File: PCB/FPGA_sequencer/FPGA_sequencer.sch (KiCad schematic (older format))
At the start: 33 parts, among them U1 ADA4940-2ACPZ-R7_a, U2 AD9648BCPZ-125, U3 DB3S406F0L, U4 DB3S406F0L

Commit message: pass capacitor add
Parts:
- 10n1, C1, C10, C11, C12, C13, C14, C15, C2, C3, C4, C5, C6, C7, C8, C9: footprint Capacitor_SMD:C_0603_1608Metric -> Capacitors_SMD:C_0603
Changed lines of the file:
@@
 F 0 "C1" V 7071 1700 50  0000 C CNN
 F 1 "22p" V 7162 1700 50  0000 C CNN
-F 2 "Capacitor_SMD:C_0603_1608Metric" H 7300 1700 50  0001 C CNN
+F 2 "Capacitors_SMD:C_0603" H 7300 1700 50  0001 C CNN
 F 3 "~" H 7300 1700 50  0001 C CNN
 	1    7300 1700
@@
 F 0 "C2" V 7571 1700 50  0000 C CNN
 F 1 "22p" V 7662 1700 50  0000 C CNN
-F 2 "Capacitor_SMD:C_0603_1608Metric" H 7800 1700 50  0001 C CNN
+F 2 "Capacitors_SMD:C_0603" H 7800 1700 50  0001 C CNN
 F 3 "~" H 7800 1700 50  0001 C CNN
 	1    7800 1700
@@
 F 0 "C11" H 3808 4704 50  0000 R CNN
 F 1 "0.1u" H 3808 4795 50  0000 R CNN
-F 2 "Capacitor_SMD:C_0603_1608Metric" H 3900 4750 50  0001 C CNN
+F 2 "Capacitors_SMD:C_0603" H 3900 4750 50  0001 C CNN
 F 3 "~" H 3900 4750 50  0001 C CNN
 	1    3900 4750
@@
 F 0 "C9" H 3508 4704 50  0000 R CNN
 F 1 "0.1u" H 3508 4795 50  0000 R CNN
-F 2 "Capacitor_SMD:C_0603_1608Metric" H 3600 4750 50  0001 C CNN
+F 2 "Capacitors_SMD:C_0603" H 3600 4750 50  0001 C CNN
 F 3 "~" H 3600 4750 50  0001 C CNN
 	1    3600 4750
@@
 F 0 "C7" H 3158 4704 50  0000 R CNN
 F 1 "0.1u" H 3158 4795 50  0000 R CNN
-F 2 "Capacitor_SMD:C_0603_1608Metric" H 3250 4750 50  0001 C CNN
+F 2 "Capacitors_SMD:C_0603" H 3250 4750 50  0001 C CNN
 F 3 "~" H 3250 4750 50  0001 C CNN
 	1    3250 4750
@@
 F 0 "C12" H 3808 5004 50  0000 R CNN
 F 1 "0.1u" H 3808 5095 50  0000 R CNN
-F 2 "Capacitor_SMD:C_0603_1608Metric" H 3900 5050 50  0001 C CNN
+F 2 "Capacitors_SMD:C_0603" H 3900 5050 50  0001 C CNN
 F 3 "~" H 3900 5050 50  0001 C CNN
 	1    3900 5050
@@
 F 0 "C10" H 3508 5004 50  0000 R CNN
 F 1 "0.1u" H 3508 5095 50  0000 R CNN
-F 2 "Capacitor_SMD:C_0603_1608Metric" H 3600 5050 50  0001 C CNN
+F 2 "Capacitors_SMD:C_0603" H 3600 5050 50  0001 C CNN
 F 3 "~" H 3600 5050 50  0001 C CNN
 	1    3600 5050
@@
 F 0 "C8" H 3158 5004 50  0000 R CNN
 F 1 "0.1u" H 3158 5095 50  0000 R CNN
-F 2 "Capacitor_SMD:C_0603_1608Metric" H 3250 5050 50  0001 C CNN
+F 2 "Capacitors_SMD:C_0603" H 3250 5050 50  0001 C CNN
 F 3 "~" H 3250 5050 50  0001 C CNN
 	1    3250 5050
@@
 F 0 "C3" H 2508 4704 50  0000 R CNN
 F 1 "10u" H 2508 4795 50  0000 R CNN
-F 2 "Capacitor_SMD:C_0603_1608Metric" H 2600 4750 50  0001 C CNN
+F 2 "Capacitors_SMD:C_0603" H 2600 4750 50  0001 C CNN
 F 3 "~" H 2600 4750 50  0001 C CNN
 	1    2600 4750
@@
 F 0 "C4" H 2508 5004 50  0000 R CNN
 F 1 "10u" H 2508 5095 50  0000 R CNN
-F 2 "Capacitor_SMD:C_0603_1608Metric" H 2600 5050 50  0001 C CNN
+F 2 "Capacitors_SMD:C_0603" H 2600 5050 50  0001 C CNN
 F 3 "~" H 2600 5050 50  0001 C CNN
 	1    2600 5050
@@
 F 0 "C5" H 2858 4704 50  0000 R CNN
 F 1 "1u" H 2858 4795 50  0000 R CNN
-F 2 "Capacitor_SMD:C_0603_1608Metric" H 2950 4750 50  0001 C CNN
+F 2 "Capacitors_SMD:C_0603" H 2950 4750 50  0001 C CNN
 F 3 "~" H 2950 4750 50  0001 C CNN
 	1    2950 4750
@@
 F 0 "C6" H 2858 5004 50  0000 R CNN
 F 1 "1u" H 2858 5095 50  0000 R CNN
-F 2 "Capacitor_SMD:C_0603_1608Metric" H 2950 5050 50  0001 C CNN
+F 2 "Capacitors_SMD:C_0603" H 2950 5050 50  0001 C CNN
 F 3 "~" H 2950 5050 50  0001 C CNN
 	1    2950 5050
@@
 F 0 "C14" H 4458 4704 50  0000 R CNN
 F 1 "10n" H 4458 4795 50  0000 R CNN
-F 2 "Capacitor_SMD:C_0603_1608Metric" H 4550 4750 50  0001 C CNN
+F 2 "Capacitors_SMD:C_0603" H 4550 4750 50  0001 C CNN
 F 3 "~" H 4550 4750 50  0001 C CNN
 	1    4550 4750
@@
 F 0 "C13" H 4158 4704 50  0000 R CNN
 F 1 "10n" H 4158 4795 50  0000 R CNN
-F 2 "Capacitor_SMD:C_0603_1608Metric" H 4250 4750 50  0001 C CNN
+F 2 "Capacitors_SMD:C_0603" H 4250 4750 50  0001 C CNN
 F 3 "~" H 4250 4750 50  0001 C CNN
 	1    4250 4750
@@
 F 0 "C15" H 4458 5004 50  0000 R CNN
 F 1 "10n" H 4458 5095 50  0000 R CNN
-F 2 "Capacitor_SMD:C_0603_1608Metric" H 4550 5050 50  0001 C CNN
+F 2 "Capacitors_SMD:C_0603" H 4550 5050 50  0001 C CNN
 F 3 "~" H 4550 5050 50  0001 C CNN
 	1    4550 5050
@@
 F 0 "10n1" H 4158 5004 50  0000 R CNN
 F 1 "0.1u" H 4158 5095 50  0000 R CNN
-F 2 "Capacitor_SMD:C_0603_1608Metric" H 4250 5050 50  0001 C CNN
+F 2 "Capacitors_SMD:C_0603" H 4250 5050 50  0001 C CNN
 F 3 "~" H 4250 5050 50  0001 C CNN
 	1    4250 5050

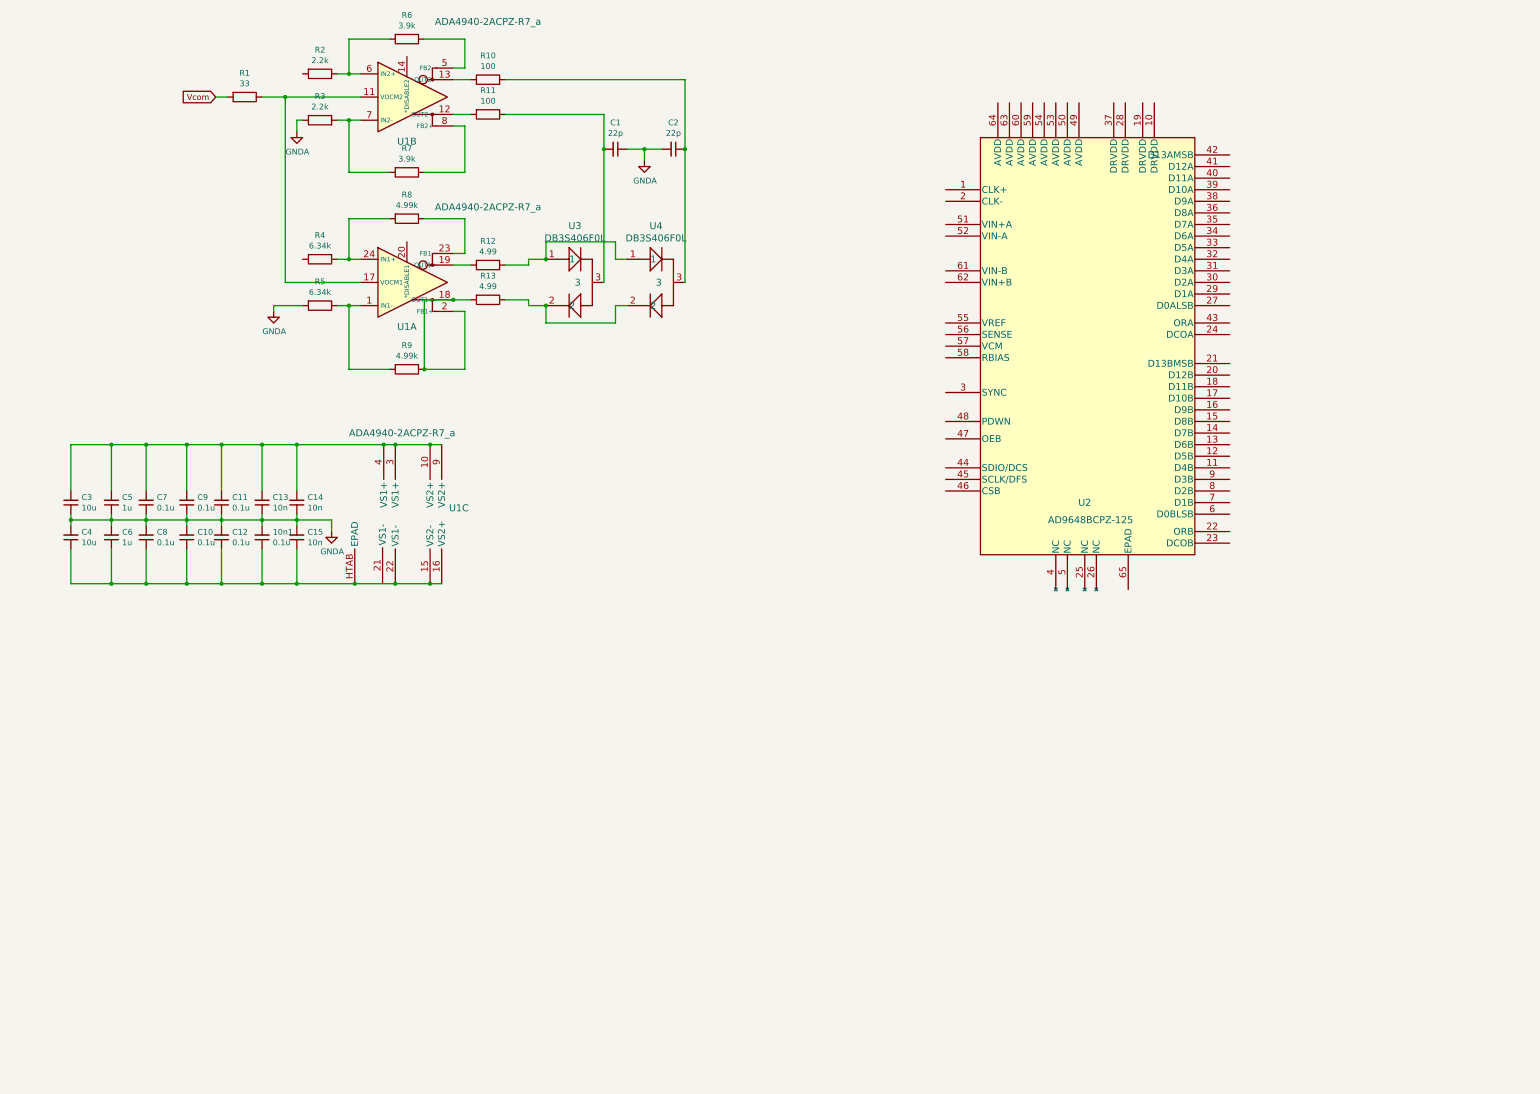
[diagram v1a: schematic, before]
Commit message: AD8065 add
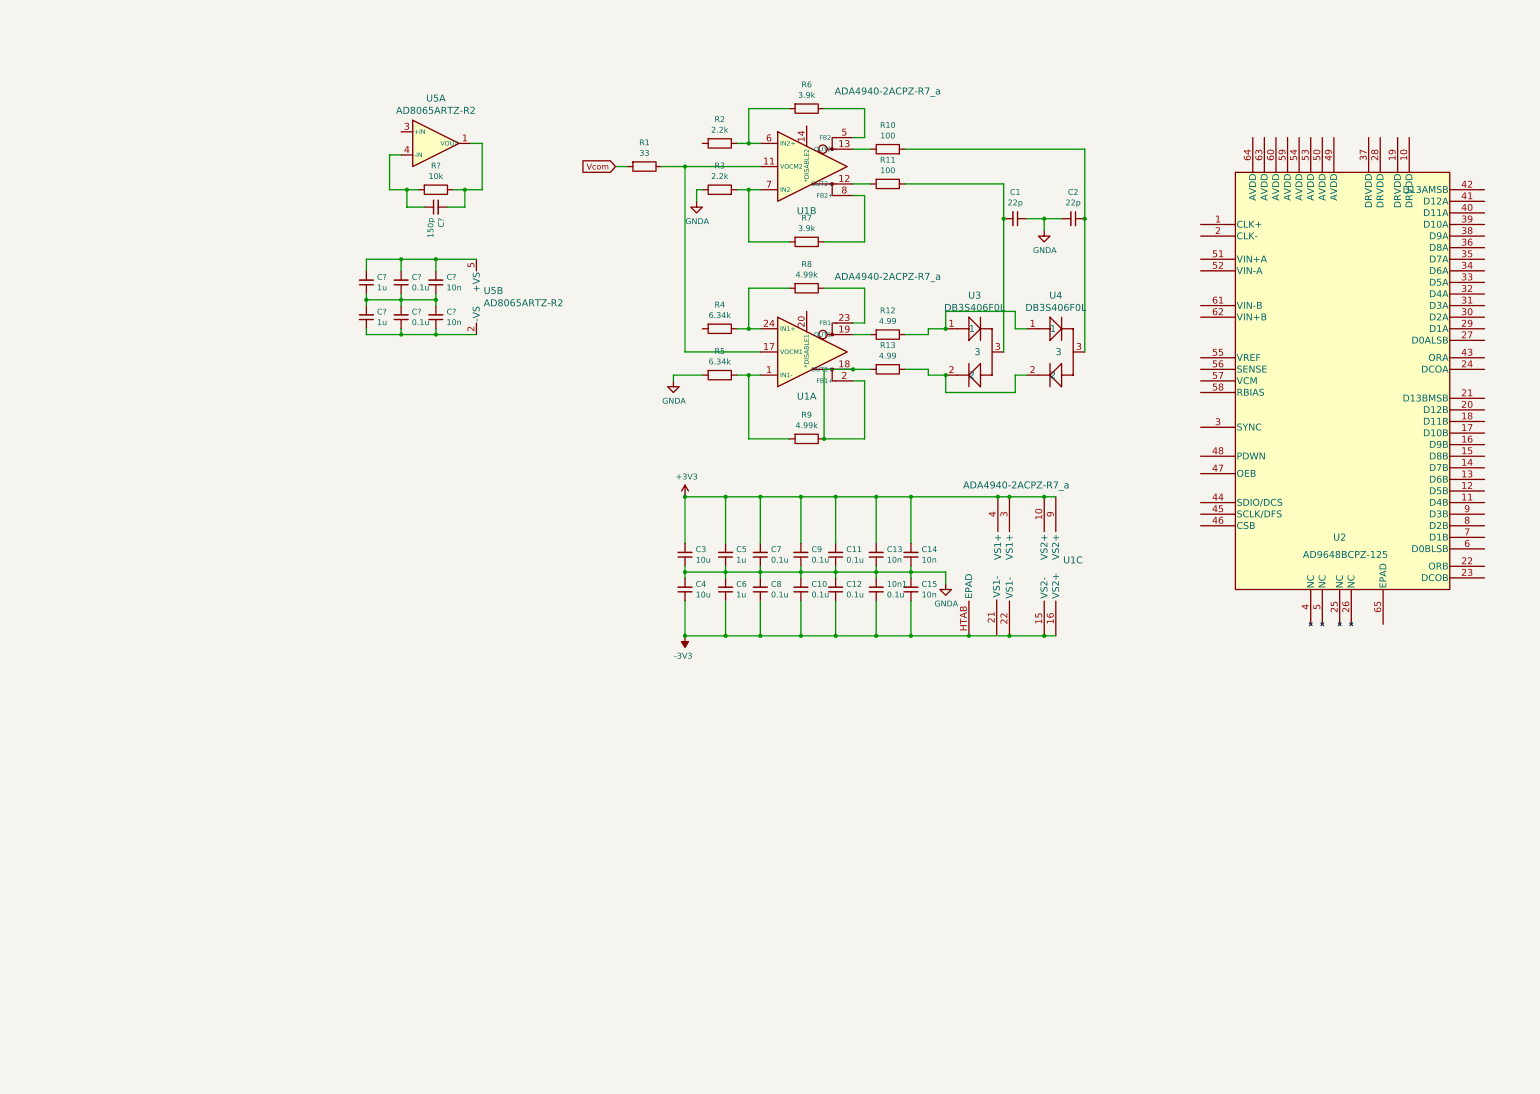
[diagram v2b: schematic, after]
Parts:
- added C? (x2): 0.1u, Capacitors_SMD:C_0603, symbol Device:C_Small
- added C? (x2): 10n, Capacitors_SMD:C_0603, symbol Device:C_Small
- added C? (x2): 1u, Capacitors_SMD:C_0603, symbol Device:C_Small
- added C?: 150p, Capacitors_SMD:C_0603, symbol Device:C_Small
- added R?: 10k, Resistor_SMD:R_0603_1608Metric, symbol Device:R
- added U5: AD8065ARTZ-R2, FPGA_sequencer:AD8065ARTZ-R2, symbol FPGA_sequencer:AD8065ARTZ-R2
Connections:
- net +3V3: now reaches C11.2, C13.2, C14.2, C3.2, C5.2, C7.2, C9.2, U1.10 (VS2+), U1.3 (VS1+), U1.4 (VS1+), U1.9 (VS2+)
- net -3V3: now reaches 10n1.1, C10.1, C12.1, C15.1, C4.1, C6.1, C8.1, U1.15 (VS2-), U1.16 (VS2+), U1.22 (VS1-), U1.HTAB (EPAD)
- new net: C?.2, R?.1, U5.1 (VOUT)
- new net: C?.1, R?.2, U5.4 (-IN)
- new net: C?.1, C?.1, C?.1, U5.2 (-VS)
- new net: C?.2, C?.2, C?.2, U5.5 (+VS)
- new net: C?.1, C?.1, C?.1, C?.2, C?.2, C?.2
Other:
- moved on the sheet: 10n1, C1, C10, C11, C12, C13, C14, C15, C2, C3, C4, C5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

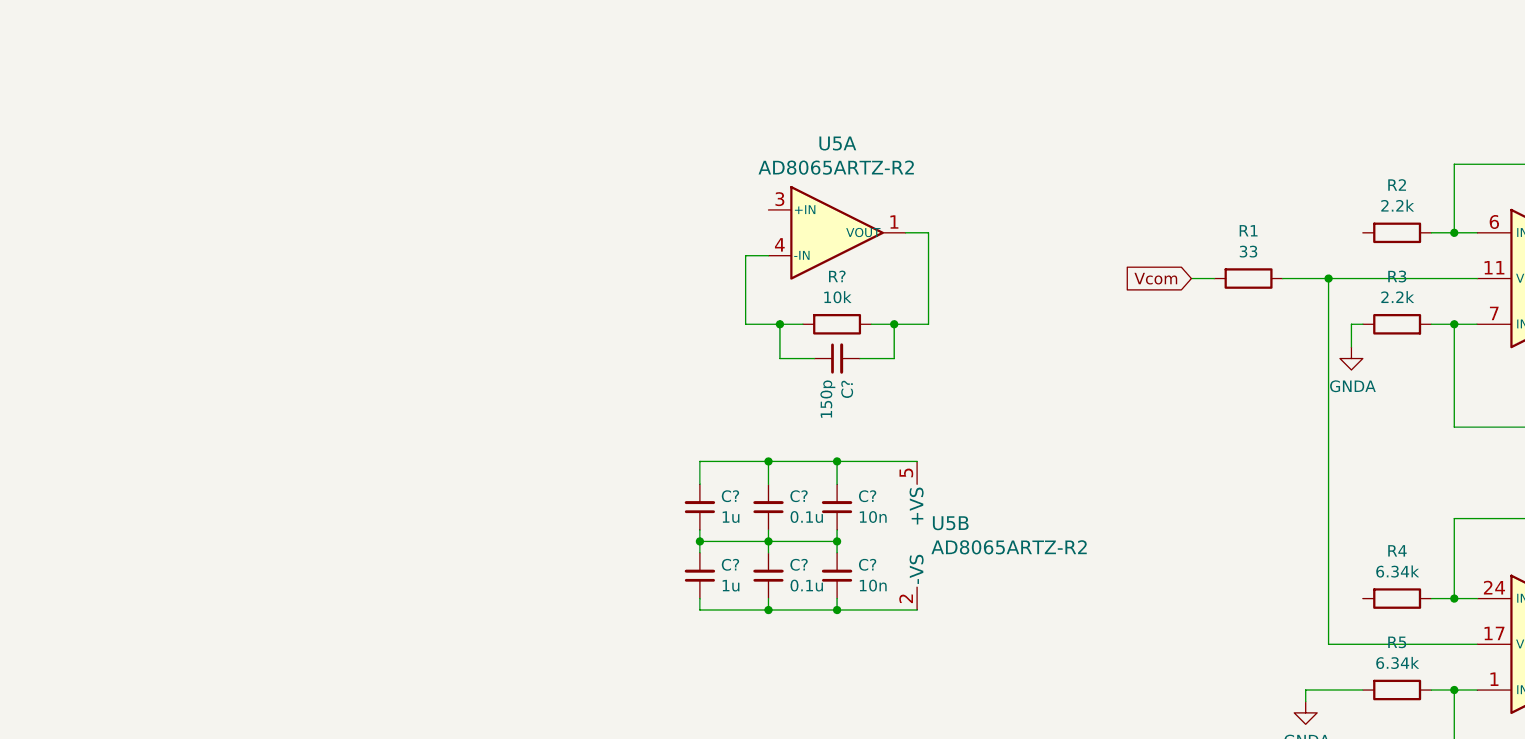
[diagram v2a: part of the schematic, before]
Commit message: MAX4565 Analog switch add
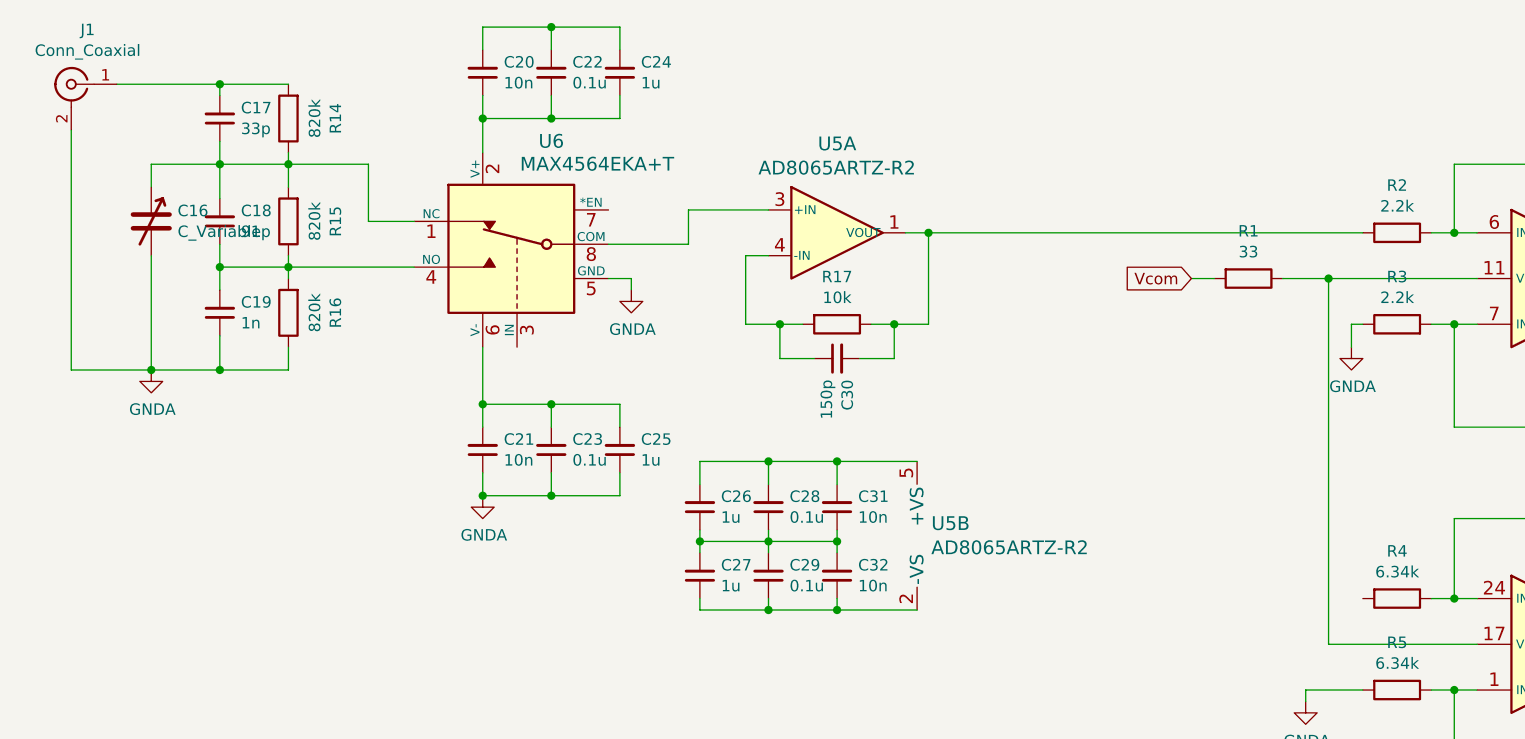
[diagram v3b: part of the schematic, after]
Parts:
- added C16: C_Variable, Capacitor_SMD:C_Trimmer_Murata_TZB4-A, symbol Device:C_Variable
- added C17: 33p, Capacitor_SMD:C_0201_0603Metric, symbol Device:C_Small
- added C18: 91p, Capacitor_SMD:C_0201_0603Metric, symbol Device:C_Small
- added C19: 1n, Capacitor_SMD:C_0201_0603Metric, symbol Device:C_Small
- added C20, C21: 10n, Capacitor_SMD:C_0201_0603Metric, symbol Device:C_Small
- added C22, C23: 0.1u, Capacitor_SMD:C_0201_0603Metric, symbol Device:C_Small
- added C24, C25: 1u, Capacitor_SMD:C_0201_0603Metric, symbol Device:C_Small
- added J1: Conn_Coaxial, Connector_Coaxial:SMA_Amphenol_132134-11_Vertical, symbol Connector:Conn_Coaxial
- added R14, R15, R16: 820k, Resistor_SMD:R_0603_1608Metric, symbol Device:R
- added U6: MAX4564EKA+T, FPGA_sequencer:MAX4564EKA&plus_T, symbol FPGA_sequencer:MAX4564EKA+T
- 10n1, C1, C10, C11, C12, C13, C14, C15, C2, C3, C4, C5, C6, C7, C8, C9: footprint Capacitors_SMD:C_0603 -> Capacitor_SMD:C_0201_0603Metric
- C26, C27, C28, C29, C30, C31, C32: renamed from C?; footprint Capacitors_SMD:C_0603 -> Capacitor_SMD:C_0201_0603Metric
- gave numbers to parts that had none: 1
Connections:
- net GNDA: now also C16.2, C19.1, C21.1, C23.1, C25.1, J1.2 (Ext), R16.1, U6.5 (GND)
- net at C30.2, R17.1, U5.1 (VOUT): now also R2.2
- net at U5.3 (+IN): now also U6.8 (COM)
- new net: C16.1, C17.1, C18.2, R14.1, R15.2, U6.1 (NC)
- new net: C20.1, C22.1, C24.1, U6.2 (V+)
- new net: C18.1, C19.2, R15.1, R16.2, U6.4 (NO)
- new net: C21.2, C23.2, C25.2, U6.6 (V-)
- new net: C17.2, J1.1 (In), R14.2
- new net: C20.2, C22.2, C24.2

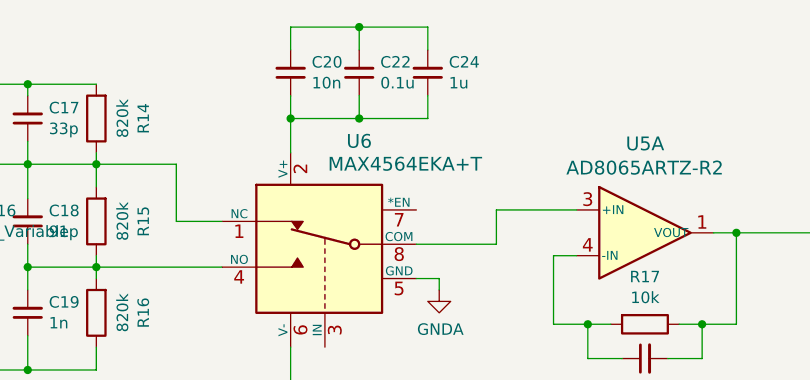
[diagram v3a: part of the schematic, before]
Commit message: ADC driver pattern write
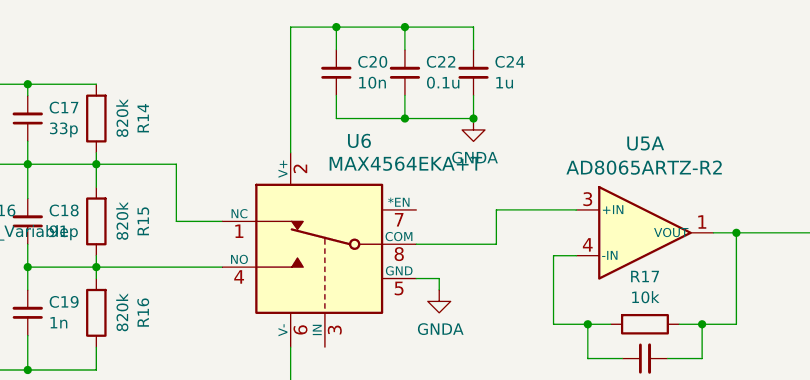
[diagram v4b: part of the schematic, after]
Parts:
- 10n1, C1, C10, C11, C12, C13, C14, C15, C17, C18, C19, C2, C20, C21, C22, C23, C24, C25, C26, C27, C28, C29, C3, C30, C31, C32, C4, C5, C6, C7, C8, C9: footprint Capacitor_SMD:C_0201_0603Metric -> Capacitor_SMD:C_0603_1608Metric
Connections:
- net GNDA: now also C20.1, C22.1, C24.1
- net at C20.2, C22.2, C24.2: now also U6.2 (V+)
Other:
- moved on the sheet: C20, C22, C24
